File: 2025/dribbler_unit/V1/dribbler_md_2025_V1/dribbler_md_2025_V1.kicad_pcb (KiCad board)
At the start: 2 copper layers, 50 x 40 mm, 101 parts, among them J1 Conn_01x02_Pin, J2 Conn_01x07_Pin, J3 Conn_01x02_Pin, J4 Conn_01x02_Pin, J5 Conn_01x02_Pin, J6 Conn_01x04_Pin, SW1 SW_Wuerth_450301014042, SW2 SW_Wuerth_450301014042, SW3 SW_MEC_5E, SW4 SW_Wuerth_450301014042, SW5 SW_MEC_5E, U1 MAX3051, U2 STS8DN3LLH5, U3 STS8DN3LLH5, U4 DRV8701, U5 STM32F446RETx, Y1 Crystal_GND2

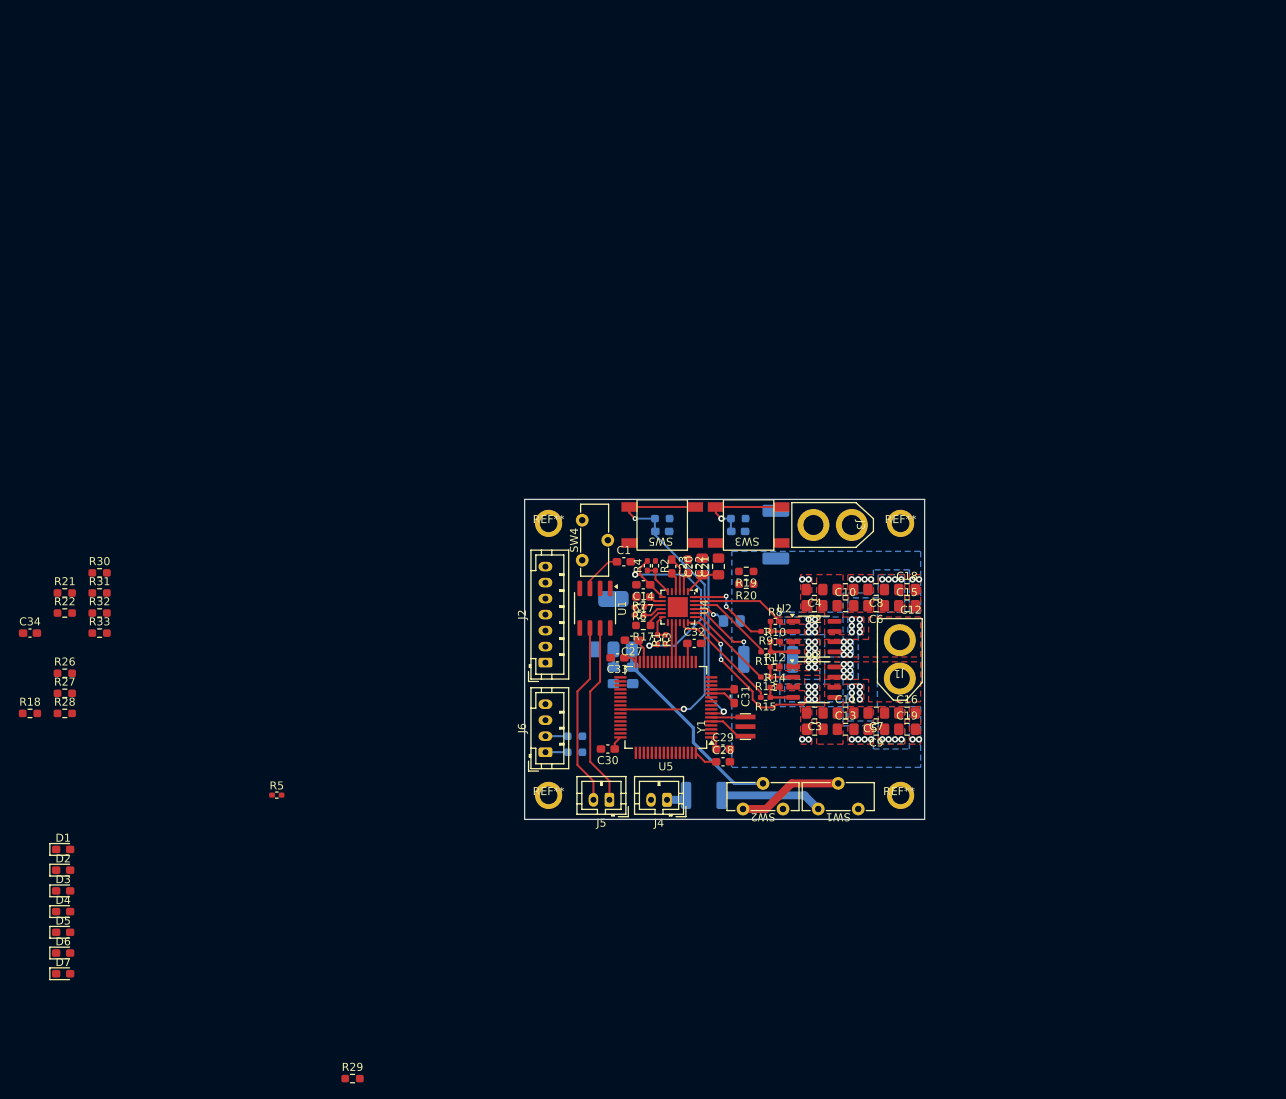
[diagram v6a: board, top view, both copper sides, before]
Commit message: 446周りを再配線
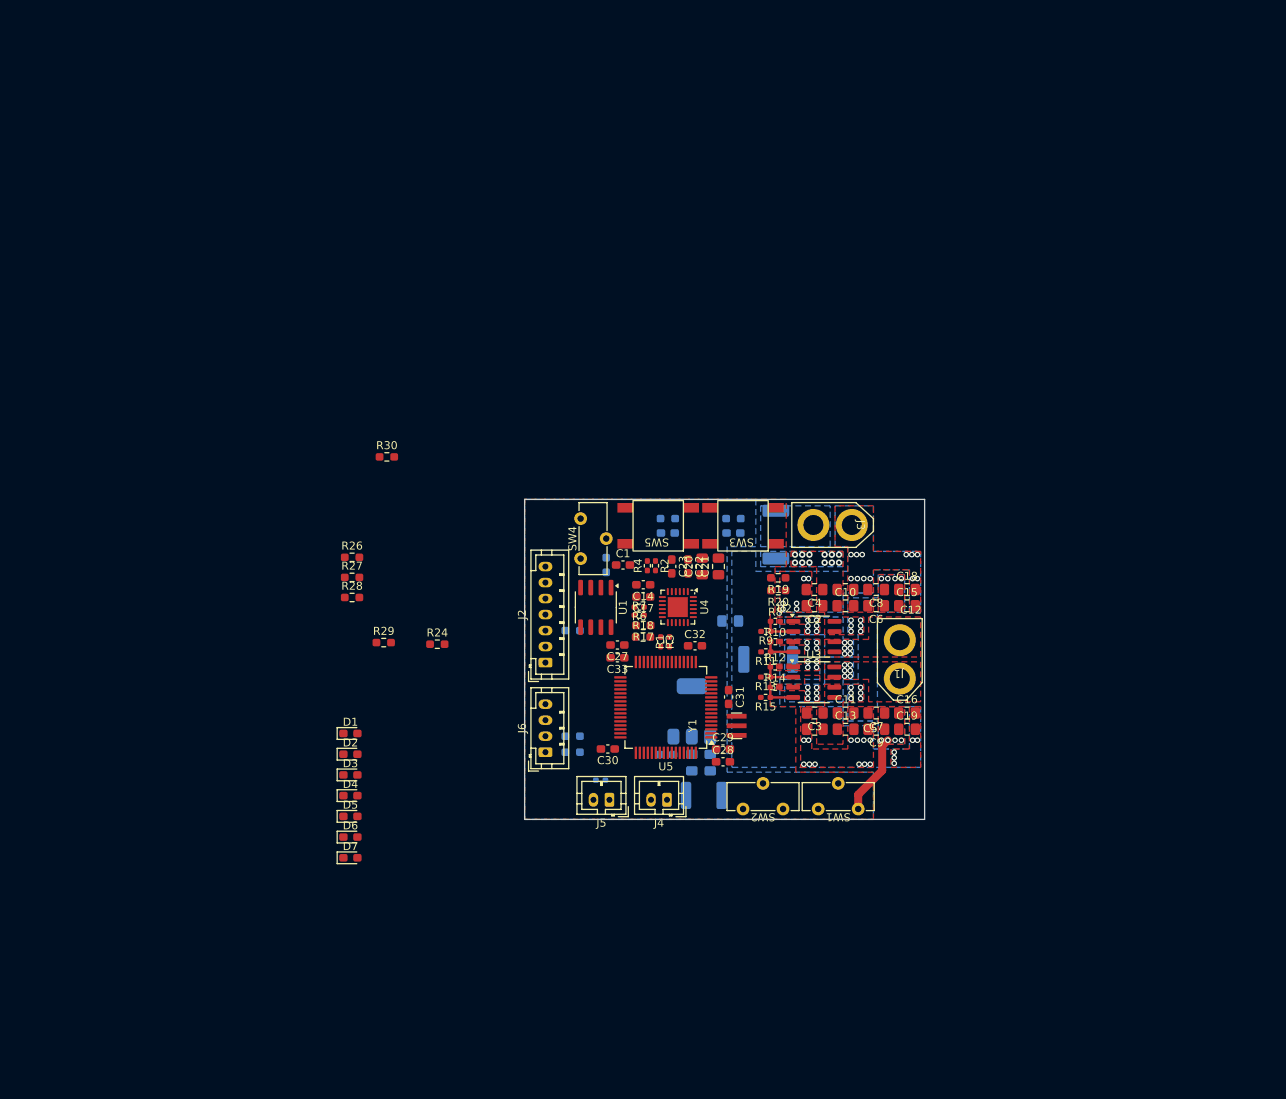
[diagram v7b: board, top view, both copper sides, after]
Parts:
- removed R33, R34: 10k, Resistor_SMD:R_0603_1608Metric_Pad0.98x0.95mm_HandSolder
- removed REF** (x4): m2 hole, dribbler_md:m2 hole
- C34, R5: moved to B.Cu
- R21, R22: value 0 -> 10k; moved to B.Cu
- R24: value 10k -> 1k; moved to F.Cu
- R25: value 10k -> 2k
- R26: value 1k -> 10k
- R27: value 2k -> 1k
- R28: value 10k -> 1k
- R31, R32: value 1k -> 10k; moved to B.Cu
- moved C34 81.0 mm to (157.7, 131.9)
- moved R18 77.2 mm to (154.8, 117.2)
- moved R32 72.0 mm to (157.9, 102.4), turned to 180 degrees
- moved R21 66.5 mm to (146.0, 131.6), turned to 180 degrees
- moved R22 65.3 mm to (146.0, 129.6)
- moved R31 63.4 mm to (150.2, 108.2), turned to -90 degrees
- moved R29 54.6 mm to (122.4, 117.9)
- moved R5 40.5 mm to (149.5, 135.1), turned to 180 degrees
- moved R26 38.7 mm to (118.4, 107.2)
- moved R27 38.7 mm to (118.4, 109.8)
- moved R28 38.7 mm to (118.4, 112.3)
- moved R30 38.7 mm to (122.8, 94.7)
- moved D1 38.7 mm to (118.2, 129.3)
- moved D2 38.7 mm to (118.2, 131.8)
- moved D3 38.7 mm to (118.2, 134.4)
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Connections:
- C25 pad 2: GND_REG -> GND_main
- C26 pad 2: GND_REG -> GND_main
- R21 pad 2: GND_REG -> ENC_1
- R22 pad 1: GND_main -> ENC_2
- R22 pad 2: GND_REG -> GND_main
- R23 pad 1: GND_main -> 3.3V_sub
- R23 pad 2: ENC_1 -> NRST
- R24 pad 1: ENC_2 -> 3.3V_sub
- R24 pad 2: GND_main -> Net-(D1-A)
- R25 pad 1: 3.3V_sub -> 6.5V_main
- R25 pad 2: NRST -> Net-(D2-A)
- R26 pad 1: 3.3V_sub -> 18V_main
- R26 pad 2: Net-(D1-A) -> Net-(D3-A)
- R27 pad 1: 6.5V_main -> USER_LED_1
- R27 pad 2: Net-(D2-A) -> Net-(D4-A)
- R28 pad 1: 18V_main -> USER_LED_2
- R28 pad 2: Net-(D3-A) -> Net-(D5-A)
- R29 pad 1: USER_LED_1 -> GL2
- R29 pad 2: Net-(D4-A) -> Net-(D6-A)
- R30 pad 1: USER_LED_2 -> GL1
- R30 pad 2: Net-(D5-A) -> Net-(D7-A)
- R31 pad 1: GL2 -> BOOT
- R31 pad 2: Net-(D6-A) -> GND_log
- R32 pad 1: GL1 -> 3.3V_sub
- R32 pad 2: Net-(D7-A) -> USER_SW
- REG1 pad 3: GND_REG -> GND_main
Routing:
- net USER_SW: track 48.3 -> 0.00 mm, vias 2 -> 0
- net NRST: track 33.6 -> 0.00 mm, vias 2 -> 0
- net Net-(U4-AVDD): track 28.3 -> 0.00 mm, vias 2 -> 0
- net Net-(REG1-VIN): track 25.7 -> 0.00 mm
- net CANH: track 23.0 -> 0.00 mm
- net CANL: track 23.0 -> 0.00 mm
- net 3.3V_sub: track 21.9 -> 0.00 mm
- net SH1: track 21.6 -> 0.00 mm, vias 14 -> 12
- net GH1: track 14.2 -> 0.00 mm
- net Net-(SW1-B): track 13.2 -> 0.00 mm
- net 6.5V_main: track 12.8 -> 0.00 mm
- net SH2: track 11.9 -> 0.00 mm
- net GL1: track 11.5 -> 0.00 mm
- net GH2: track 11.1 -> 0.00 mm, vias 2 -> 0
- net GL2: track 11.1 -> 0.00 mm
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- added copper zone on B.Cu, net GND_log
- added copper zone on F.Cu, net GND_log
- added copper zone on B.Cu, net Net-(J3-Pin_1)

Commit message: 配線完了
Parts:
- removed D3, D6, D7: LED, LED_SMD:LED_0603_1608Metric_Pad1.05x0.95mm_HandSolder
- removed R26: 10k, Resistor_SMD:R_0603_1608Metric_Pad0.98x0.95mm_HandSolder
- removed R29, R30: 1k, Resistor_SMD:R_0603_1608Metric_Pad0.98x0.95mm_HandSolder
- added REF**: m2 hole, dribbler_md:m2 hole, F.Cu at (143.0, 137.0)
- added REF**: m2 hole, dribbler_md:m2 hole, F.Cu at (187.0, 103.0)
- added REF**: m2 hole, dribbler_md:m2 hole, F.Cu at (187.0, 137.0)
- added REF**: m2 hole, dribbler_md:m2 hole, F.Cu at (143.0, 103.0)
- R25: moved to F.Cu
- moved R28 56.7 mm to (171.7, 131.7), turned to 90 degrees
- moved R27 56.1 mm to (170.1, 131.7), turned to 90 degrees
- moved D5 54.7 mm to (171.7, 128.3), turned to -90 degrees
- moved D1 52.9 mm to (167.6, 110.3)
- moved D4 52.6 mm to (170.1, 128.3), turned to -90 degrees
- moved D2 44.5 mm to (162.3, 137.8), turned to 180 degrees
- moved R24 39.0 mm to (167.6, 111.8)
- moved R25 34.0 mm to (162.4, 136.2)
- moved R23 24.5 mm to (166.1, 102.4)
- moved C34 7.79 mm to (159.8, 124.4), turned to -90 degrees
- moved REG1 6.34 mm to (167.2, 127.2), turned to 0 degrees
- moved C26 5.70 mm to (160.9, 127.2), turned to 180 degrees
- moved C25 4.02 mm to (160.9, 129.6), turned to 180 degrees
- moved R22 2.31 mm to (145.8, 131.9)
- moved R21 1.81 mm to (145.8, 133.4)
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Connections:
- D1 pad 1: GND_main -> GND_log
- D2 pad 1: GND_main -> GND_log
- J6 pad 4: GND_main -> GND_log
- R21 pad 1: GND_main -> GND_log
- R22 pad 2: GND_main -> GND_log
- REG1 pad 4: (no net) -> GND_main
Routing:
- net 3.3V_sub: track 0.00 -> 157.7 mm, vias 0 -> 14
- net GND_log: track 0.00 -> 66.4 mm, vias 0 -> 34
- net NRST: track 0.00 -> 64.7 mm, vias 0 -> 3
- net BOOT: track 0.00 -> 49.7 mm
- net CAN1_TX: track 0.00 -> 46.5 mm
- net USER_SW: track 0.00 -> 43.3 mm, vias 0 -> 1
- net GND_main: track 0.00 -> 41.8 mm, vias 35 -> 36
- net CAN1_RX: track 0.00 -> 37.7 mm
- net ENC_1: track 0.00 -> 29.8 mm, vias 0 -> 2
- net SWCLK: track 0.00 -> 28.9 mm, vias 0 -> 1
- net 18V_main: track 10.1 -> 37.0 mm, vias 32 -> 35
- net MD_nSLEEP: track 0.00 -> 25.0 mm, vias 0 -> 2
- net CANH: track 0.00 -> 24.3 mm, vias 0 -> 1
- net CANL: track 0.00 -> 23.5 mm, vias 0 -> 1
- net ENC_2: track 0.00 -> 22.7 mm, vias 0 -> 1
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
